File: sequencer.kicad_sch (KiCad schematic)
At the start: 77 parts, among them J1 AudioJack2_SwitchT, J2 AudioJack2_SwitchT, J3 AudioJack2_SwitchT, J4 Conn_ARM_JTAG_SWD_10, J5 Conn_01x06_Male, J6 Conn_01x02_Male, SW1 OS102011MS2QN1, SW10 EG1206A, SW2 OS102011MS2QN1, SW3 OS102011MS2QN1, SW4 OS102011MS2QN1, SW5 OS102011MS2QN1, SW6 OS102011MS2QN1, SW7 OS102011MS2QN1, SW8 OS102011MS2QN1, SW9 OS102011MS2QN1, U1 LM358, U2 74HC4051, U3 STM32F031K6Tx, U4 74HCT14, U5 L78L05_SOT89, U6 L78L33_SOT89, X1 ASV-8.000MHz

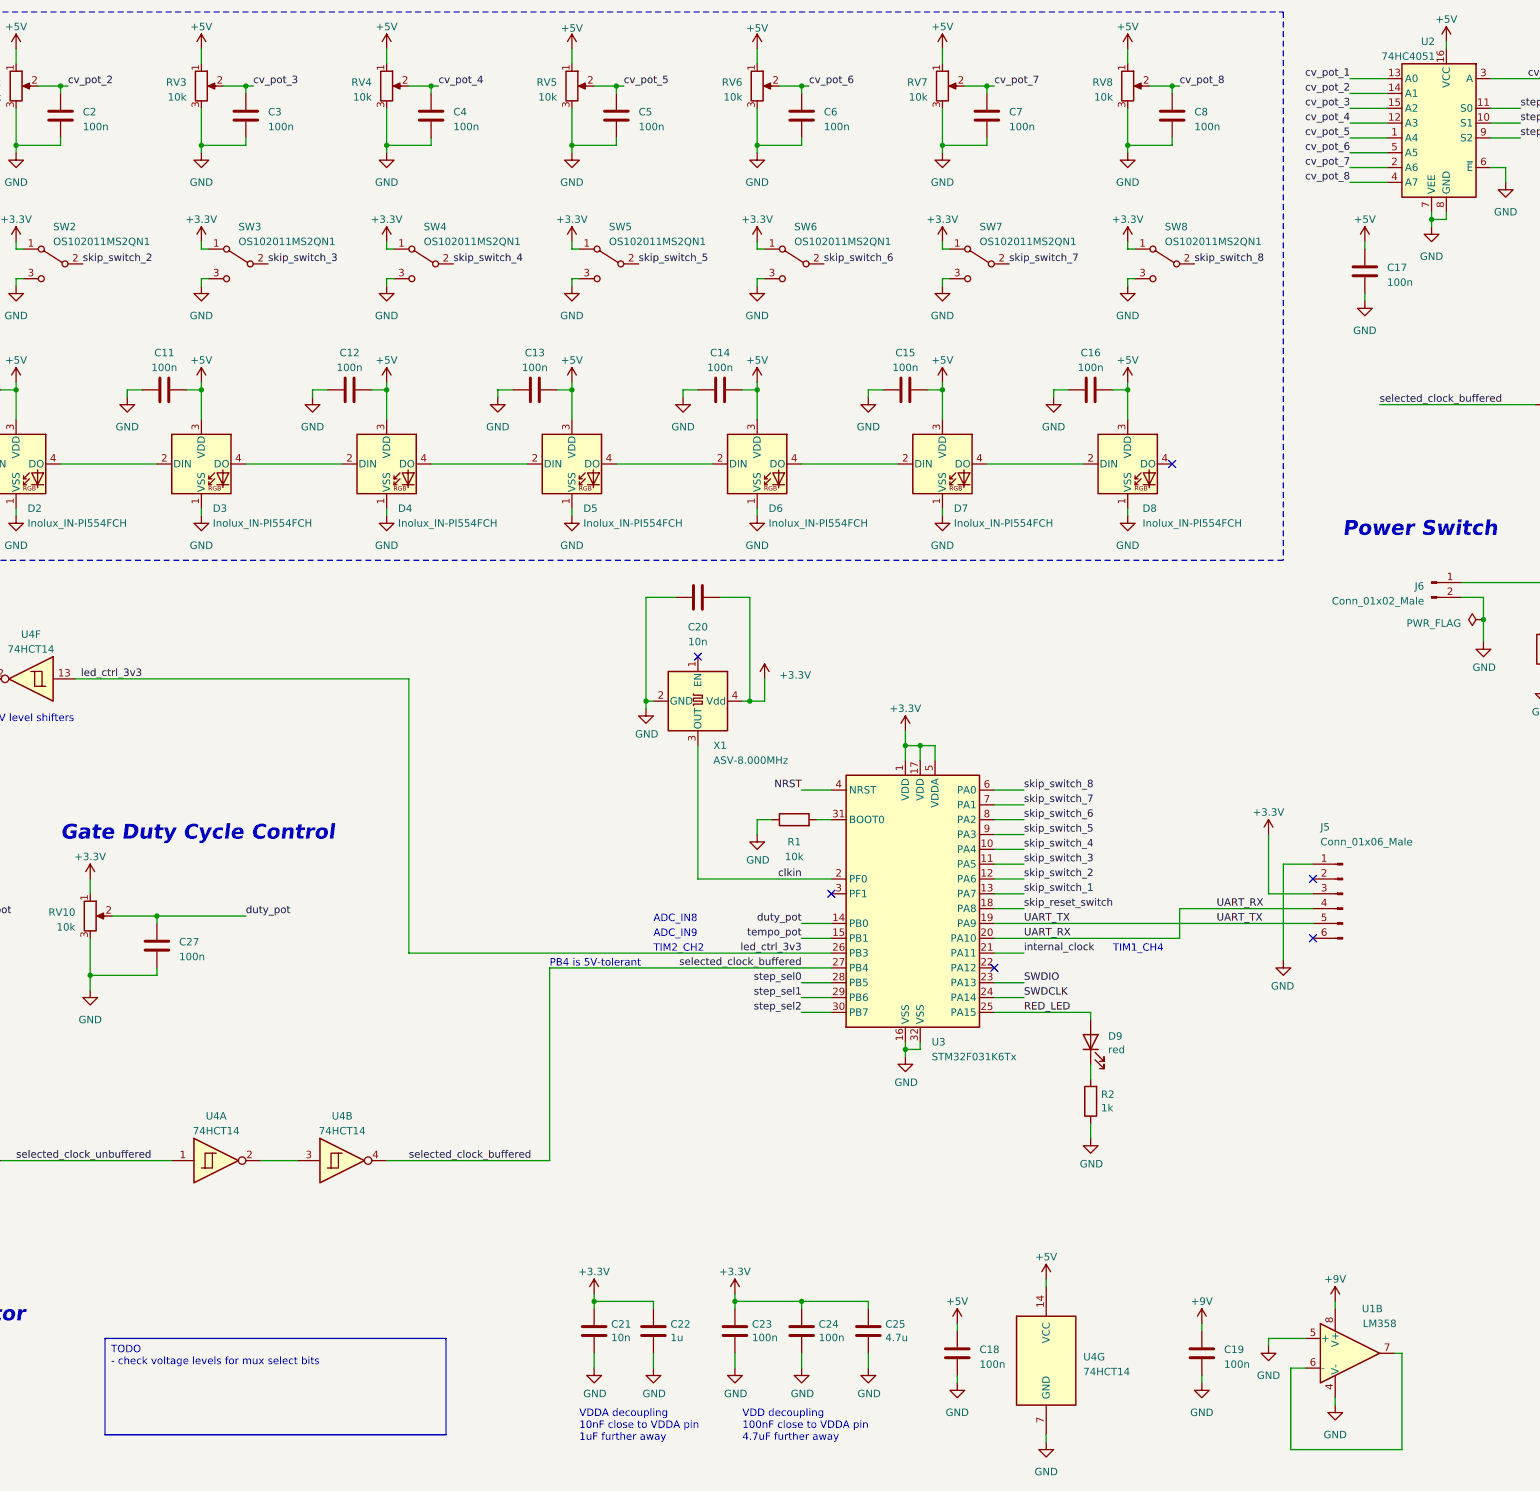
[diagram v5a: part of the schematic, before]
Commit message: change analog switch to HCT
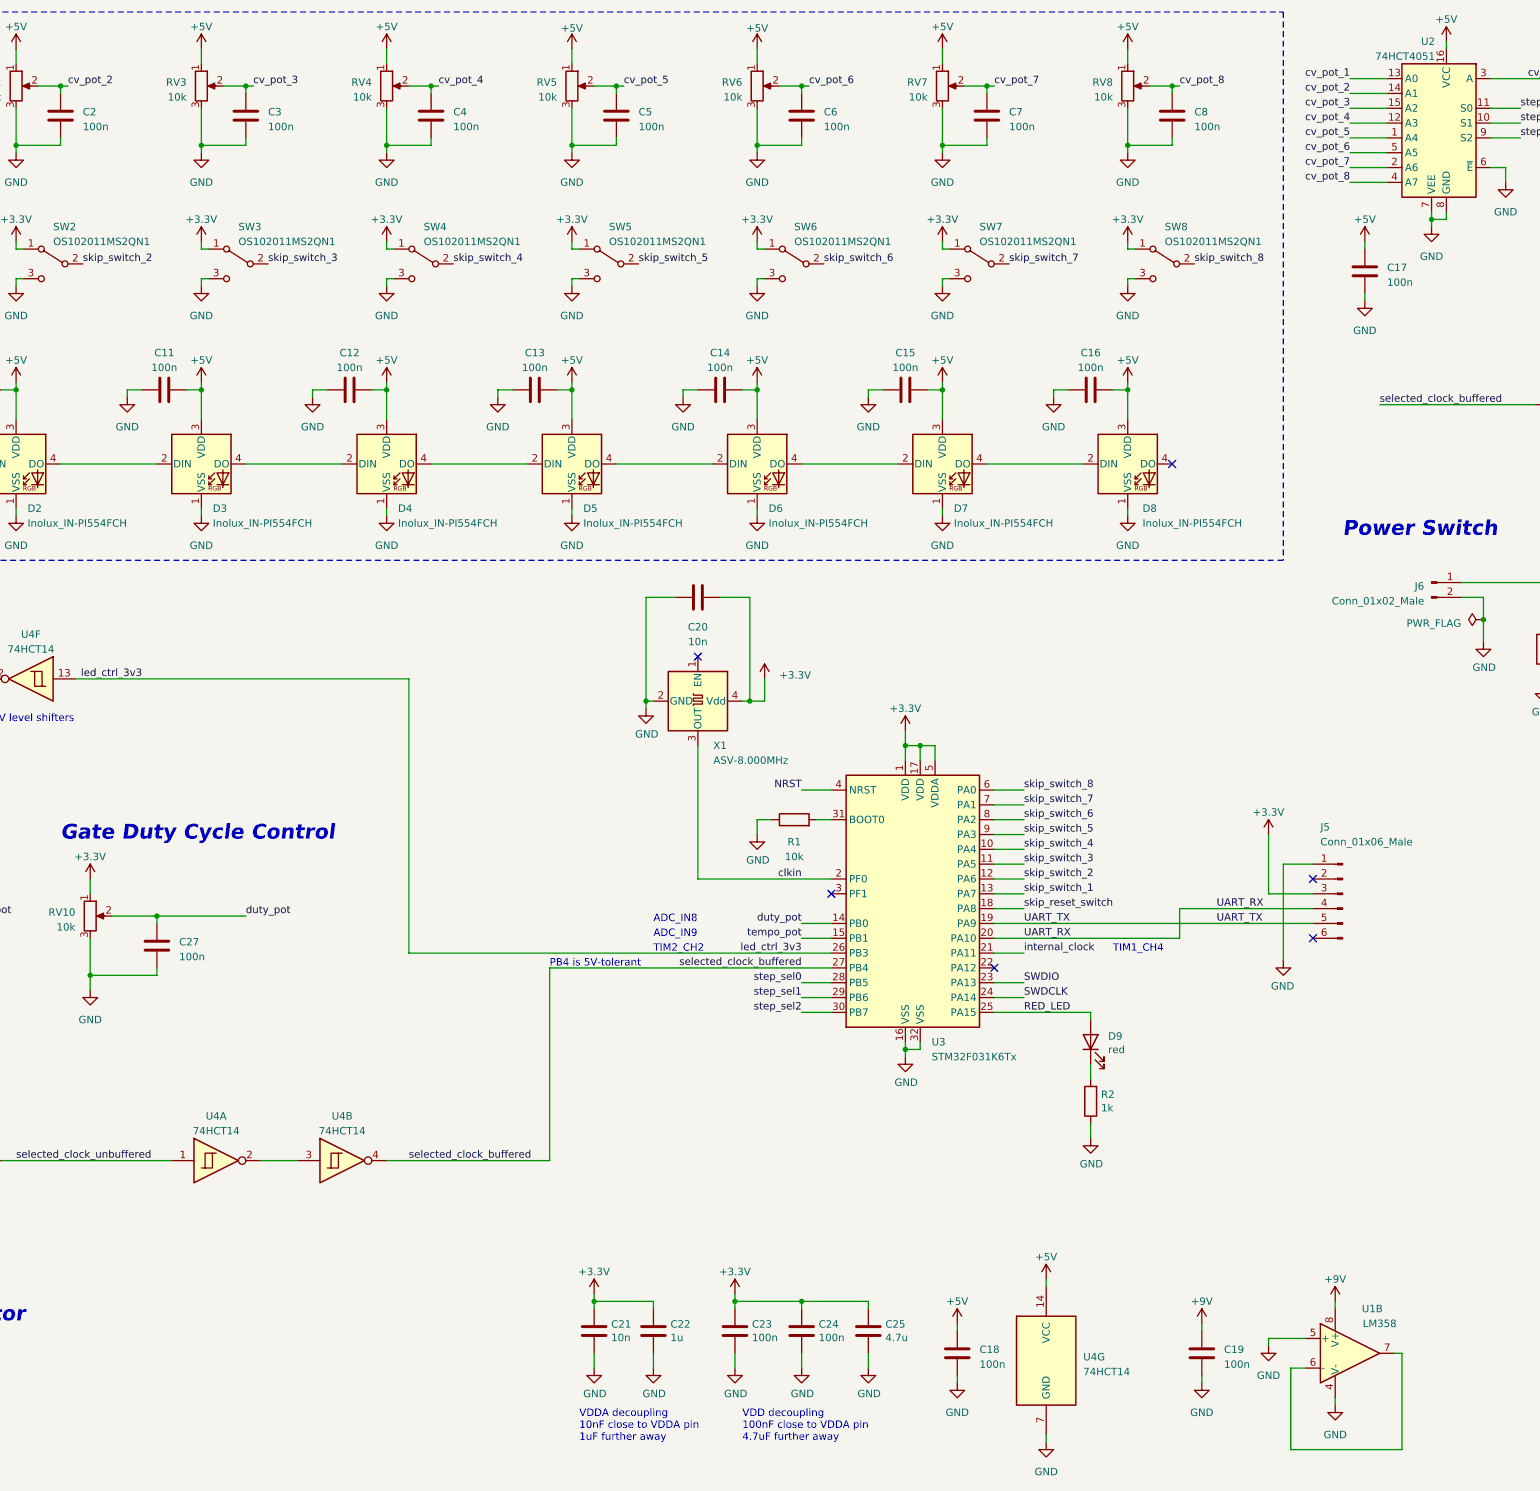
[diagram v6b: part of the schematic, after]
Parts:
- U2: value 74HC4051 -> 74HCT4051
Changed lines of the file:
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@@
     (fill (type none))
-  )
-  (text_box "TODO\n- check voltage levels for mux select bits"
-    (at 82.55 241.3 0) (size 58.42 16.51)
-    (stroke (width 0) (type default))
-    (fill (type none))
-    (effects (font (size 1.27 1.27)) (justify left top))
   )
   (text "ADC_IN9" (at 176.53 172.72 0)
@@
       (effects (font (size 1.27 1.27)) (justify left))
     )
-    (property "Value" "74HC4051" (at 310.4641 21.59 0)
+    (property "Value" "74HCT4051" (at 310.4641 21.59 0)
       (effects (font (size 1.27 1.27)) (justify left))
     )

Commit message: r0 fab
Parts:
- added LOGO1: CC-BY-SA_0.33in, Symbol_CreativeCommons:CC-BY-SA_SilkScreenTop_Small, symbol Creative_Commons:CC-BY-SA_0.33in
- added LOGO2: Logo_MadeWithKiCad, Symbol:KiCad-Logo2_5mm_SilkScreen, symbol Graphic_gkeeth:Logo_MadeWithKiCad
- added LOGO3: Logo_Open_Hardware_Small, Symbol:OSHW-Logo2_7.3x6mm_SilkScreen, symbol Graphic:Logo_Open_Hardware_Small
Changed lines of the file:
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@@
     )
   )
+  (symbol (lib_id "Graphic:Logo_Open_Hardware_Small") (at 393.7 243.84 0) (unit 1)
+    (in_bom no) (on_board yes) (dnp no) (fields_autoplaced)
+    (property "Reference" "LOGO3" (at 393.7 236.855 0)
+      (effects (font (size 1.27 1.27)) hide)
+    )
+    (property "Value" "Logo_Open_Hardware_Small" (at 393.7 249.555 0)
+      (effects (font (size 1.27 1.27)) hide)
+    )
+    (property "Footprint" "Symbol:OSHW-Logo2_7.3x6mm_SilkScreen" (at 393.7 243.84 0)
+      (effects (font (size 1.27 1.27)) hide)
+    )
+    (property "Datasheet" "~" (at 393.7 243.84 0)
+      (effects (font (size 1.27 1.27)) hide)
+    )
+    (property "Sim.Enable" "0" (at 393.7 243.84 0)
+      (effects (font (size 1.27 1.27)) hide)
+    )
+    (property "Project FNT" "" (at 393.7 243.84 0)
+      (effects (font (size 1.27 1.27)) hide)
+    )
+    (property "Manufacturer" "" (at 393.7 243.84 0)
+      (effects (font (size 1.27 1.27)) hide)
+    )
+    (property "Manufacturer PN" "" (at 393.7 243.84 0)
+      (effects (font (size 1.27 1.27)) hide)
+    )
+    (property "Distributor" "" (at 393.7 243.84 0)
+      (effects (font (size 1.27 1.27)) hide)
+    )
+    (property "Distributor PN" "" (at 393.7 243.84 0)
+      (effects (font (size 1.27 1.27)) hide)
+    )
+    (instances
+      (project "sequencer"
+        (path "/bbdda03d-2864-473b-99a3-acb9c1fabb00"
+          (reference "LOGO3") (unit 1)
+        )
+      )
+    )
+  )
   (symbol (lib_id "Regulator_Linear:L78L33_SOT89") (at 374.65 146.05 0) (unit 1)
     (in_bom yes) (on_board yes) (dnp no) (fields_autoplaced)
@@
     )
   )
+  (symbol (lib_id "Creative_Commons:CC-BY-SA_0.33in") (at 361.95 242.57 0) (unit 1)
+    (in_bom yes) (on_board yes) (dnp no) (fields_autoplaced)
+    (property "Reference" "LOGO1" (at 361.95 246.0244 0)
+      (effects (font (size 1.524 1.524)) hide)
+    )
+    (property "Value" "CC-BY-SA_0.33in" (at 361.95 239.1156 0)
+      (effects (font (size 1.524 1.524)) hide)
+    )
+    (property "Footprint" "Symbol_CreativeCommons:CC-BY-SA_SilkScreenTop_Small" (at 361.95 242.57 0)
+      (effects (font (size 1.27 1.27)) hide)
+    )
+    (property "Datasheet" "" (at 361.95 242.57 0)
+      (effects (font (size 1.27 1.27)) hide)
+    )
+    (instances
+      (project "sequencer"
+        (path "/bbdda03d-2864-473b-99a3-acb9c1fabb00"
+          (reference "LOGO1") (unit 1)
+        )
+      )
+    )
+  )
   (symbol (lib_id "Device:R") (at 251.46 200.66 180) (unit 1)
     (in_bom yes) (on_board yes) (dnp no)
@@
         )
       )
+    )
+  )
+  (symbol (lib_id "Graphic_gkeeth:Logo_MadeWithKiCad") (at 326.39 242.57 0) (unit 1)
+    (in_bom yes) (on_board yes) (dnp no) (fields_autoplaced)
+    (property "Reference" "LOGO2" (at 326.39 242.57 0)
+      (effects (font (size 1.27 1.27)) hide)
+    )
+    (property "Value" "Logo_MadeWithKiCad" (at 326.39 242.57 0)
+      (effects (font (size 1.27 1.27)) hide)
+    )
+    (property "Footprint" "Symbol:KiCad-Logo2_5mm_SilkScreen" (at 326.39 242.57 0)
+      (effects (font (size 1.27 1.27)) hide)
+    )
+    (property "Datasheet" "" (at 326.39 242.57 0)
+      (effects (font (size 1.27 1.27)) hide)
+    )
+    (instances
+      (project "sequencer"
+        (path "/bbdda03d-2864-473b-99a3-acb9c1fabb00"
+          (reference "LOGO2") (unit 1)
+        )
+      )
